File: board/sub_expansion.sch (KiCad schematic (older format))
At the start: 0 parts

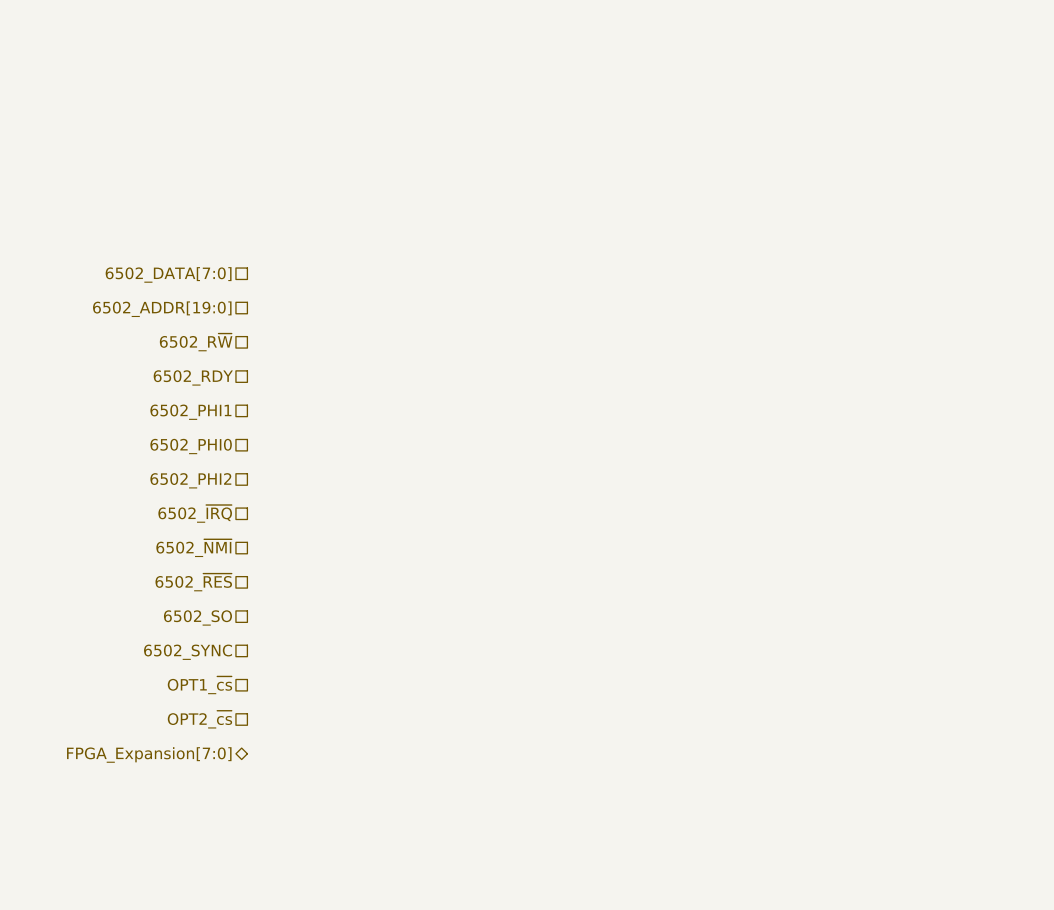
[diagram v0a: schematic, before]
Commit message: Level converters complete, display almost done
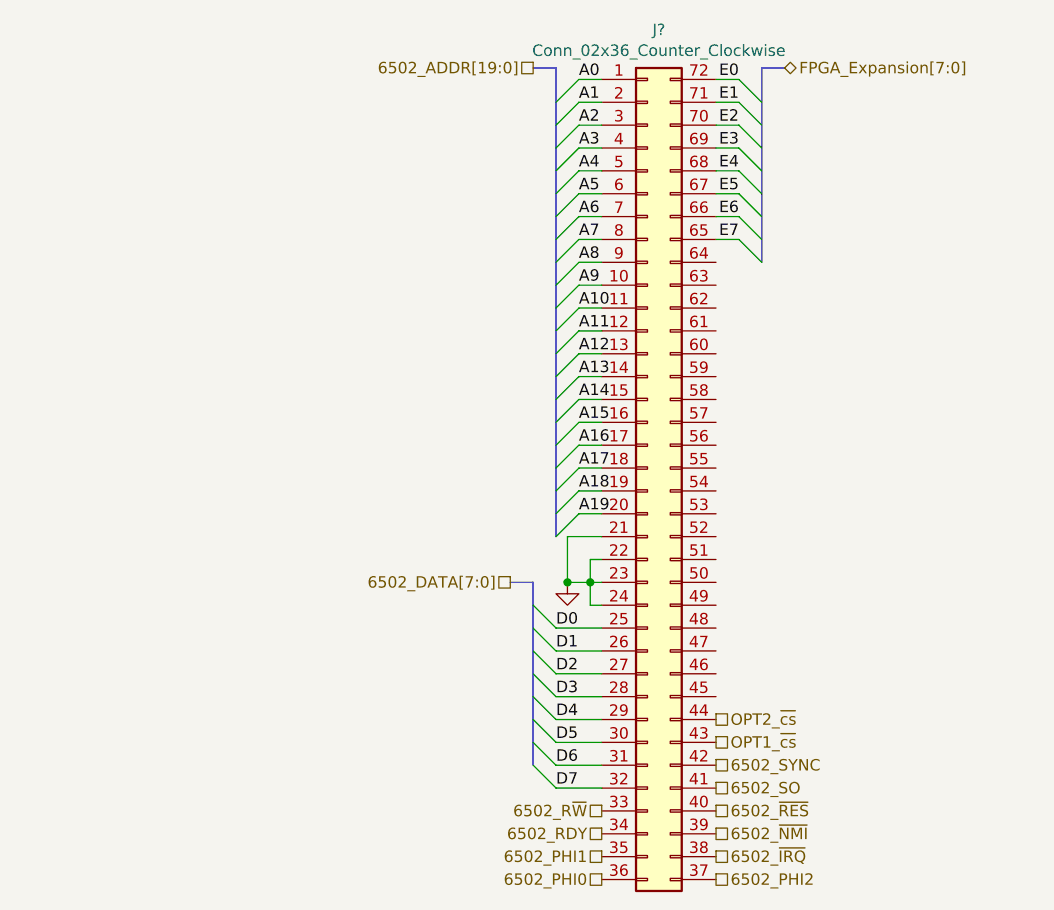
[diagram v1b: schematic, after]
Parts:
- added J?: Conn_02x36_Counter_Clockwise, symbol Connector_Generic:Conn_02x36_Counter_Clockwise
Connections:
- net 6502_PHI0: now also J?.36 (Pin_36)
- net 6502_PHI1: now also J?.35 (Pin_35)
- net 6502_PHI2: now also J?.37 (Pin_37)
- net 6502_RDY: now also J?.34 (Pin_34)
- net 6502_R~W: now also J?.33 (Pin_33)
- net 6502_SO: now also J?.41 (Pin_41)
- net 6502_SYNC: now also J?.42 (Pin_42)
- net 6502_~IRQ: now also J?.38 (Pin_38)
- net 6502_~NMI: now also J?.39 (Pin_39)
- net 6502_~RES: now also J?.40 (Pin_40)
- net OPT1_~cs: now also J?.43 (Pin_43)
- net OPT2_~cs: now also J?.44 (Pin_44)
- new net A0: J?.1 (Pin_1)
- new net A1: J?.2 (Pin_2)
- new net A10: J?.11 (Pin_11)
- new net A11: J?.12 (Pin_12)
- new net A12: J?.13 (Pin_13)
- new net A13: J?.14 (Pin_14)
- new net A14: J?.15 (Pin_15)
- new net A15: J?.16 (Pin_16)
- new net A16: J?.17 (Pin_17)
- new net A17: J?.18 (Pin_18)
- new net A18: J?.19 (Pin_19)
- new net A19: J?.20 (Pin_20)
- new net A2: J?.3 (Pin_3)
- new net A3: J?.4 (Pin_4)
- new net A4: J?.5 (Pin_5)
- new net A5: J?.6 (Pin_6)
- new net A6: J?.7 (Pin_7)
- new net A7: J?.8 (Pin_8)
- new net A8: J?.9 (Pin_9)
- new net A9: J?.10 (Pin_10)
- new net D0: J?.25 (Pin_25)
- new net D1: J?.26 (Pin_26)
- new net D2: J?.27 (Pin_27)
- new net D3: J?.28 (Pin_28)
- new net D4: J?.29 (Pin_29)
- new net D5: J?.30 (Pin_30)
- new net D6: J?.31 (Pin_31)
- new net D7: J?.32 (Pin_32)
- new net E0: J?.72 (Pin_72)
- new net E1: J?.71 (Pin_71)
- new net E2: J?.70 (Pin_70)
- new net E3: J?.69 (Pin_69)
- new net E4: J?.68 (Pin_68)
- new net E5: J?.67 (Pin_67)
- new net E6: J?.66 (Pin_66)
- new net E7: J?.65 (Pin_65)
- new net GND: J?.21 (Pin_21), J?.22 (Pin_22), J?.23 (Pin_23), J?.24 (Pin_24)

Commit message: More Schematic progress
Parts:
- gave numbers to parts that had none: 1
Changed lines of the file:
@@
 $Descr A4 11693 8268
 encoding utf-8
-Sheet 11 15
+Sheet 10 14
 Title ""
 Date ""
@@
 FPGA_Expansion[7:0]
 $Comp
-L Connector_Generic:Conn_02x36_Counter_Clockwise J?
+L Connector_Generic:Conn_02x36_Counter_Clockwise J1001
 U 1 1 5AB66C6D
 P 5950 4400
-F 0 "J?" H 6000 6317 50  0000 C CNN
+F 0 "J1001" H 6000 6317 50  0000 C CNN
 F 1 "Conn_02x36_Counter_Clockwise" H 6000 6226 50  0000 C CNN
 F 2 "" H 5950 4400 50  0001 C CNN
@@
 	5350 4900 5450 4900
 $Comp
-L power:GND #PWR?
+L power:GND #PWR01001
 U 1 1 5AB6DD73
 P 5600 4900
-F 0 "#PWR?" H 5600 4650 50  0001 C CNN
+F 0 "#PWR01001" H 5600 4650 50  0001 C CNN
 F 1 "GND" H 5500 5000 50  0001 C CNN
 F 2 "" H 5600 4900 50  0001 C CNN
@@
 	6450 2650 6550 2650
 Wire Bus Line
+	6450 2650 6450 3500
+Wire Bus Line
 	5450 4900 5450 5700
 Wire Bus Line
-	6450 2650 6450 3500
-Wire Bus Line
 	5550 2650 5550 4700

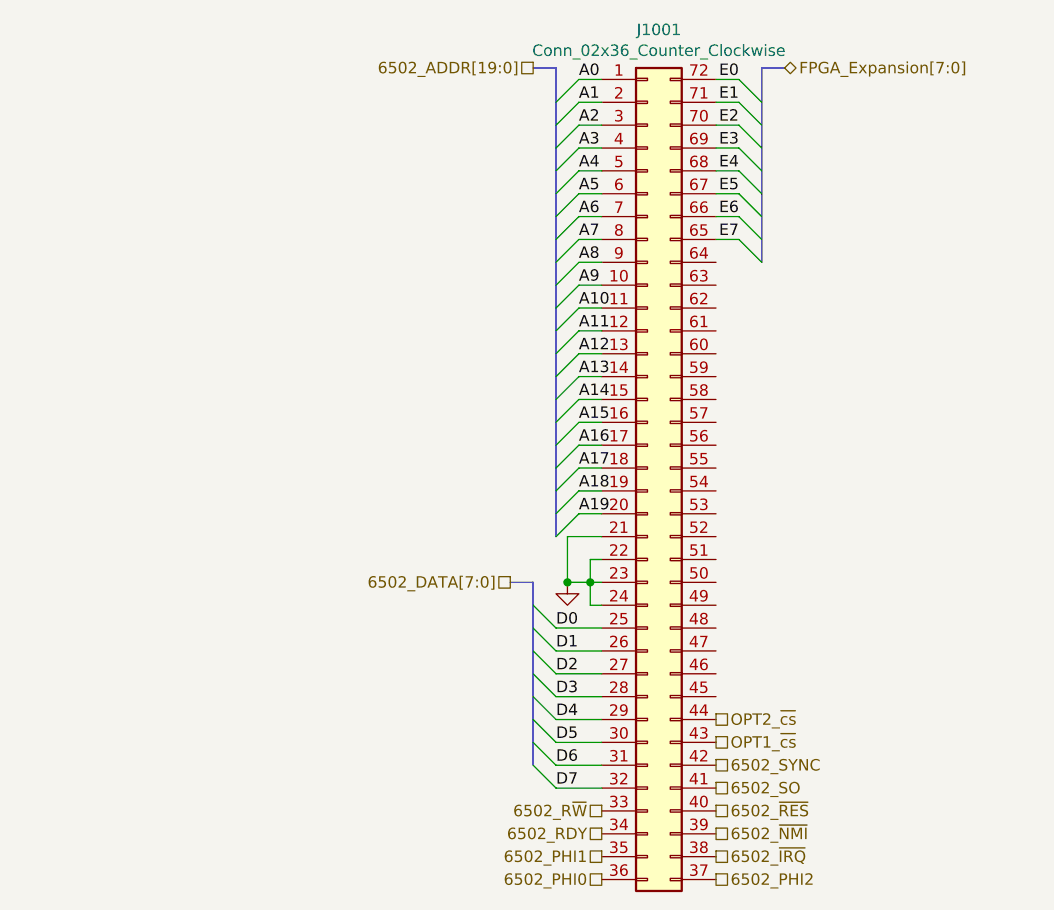
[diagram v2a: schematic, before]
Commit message: Bus signal connectivity rebuilt
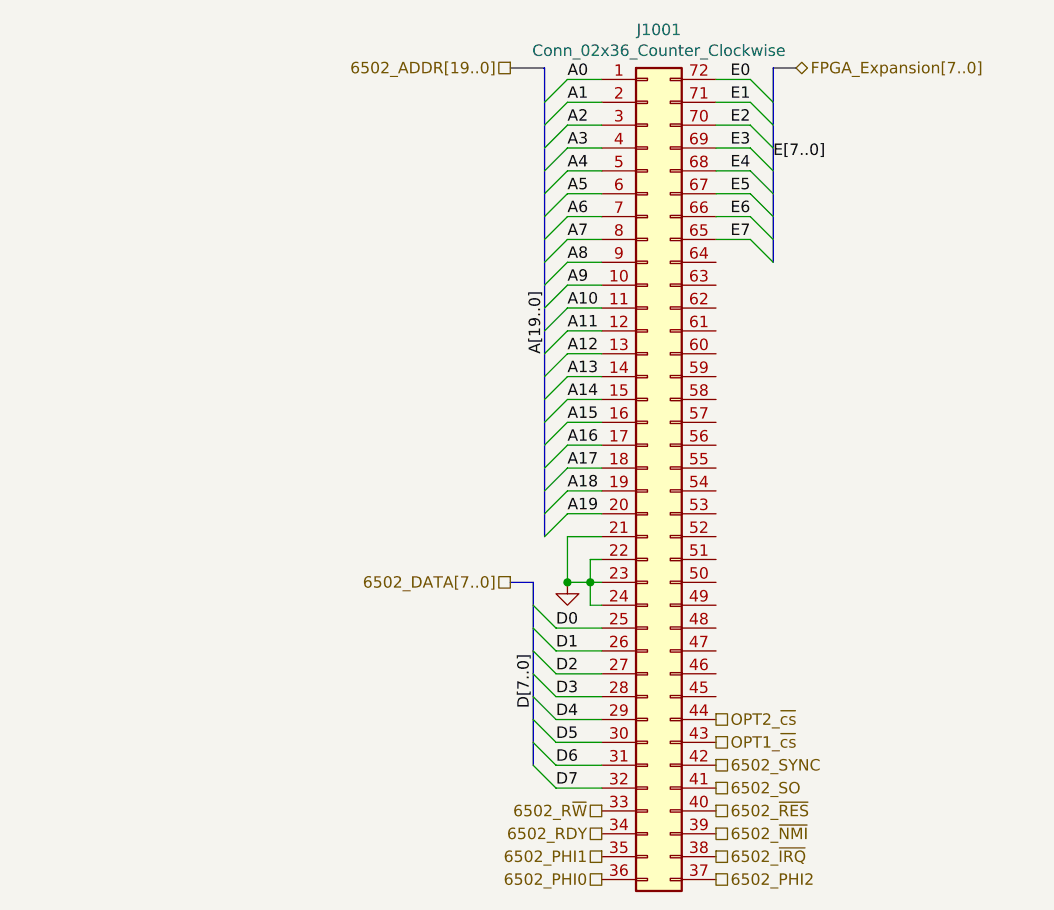
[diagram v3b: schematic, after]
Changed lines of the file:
@@
 $EndDescr
 Text HLabel 5350 4900 0    50   UnSpc ~ 0
-6502_DATA[7:0]
-Text HLabel 5450 2650 0    50   UnSpc ~ 0
-6502_ADDR[19:0]
+6502_DATA[7..0]
+Text HLabel 5350 2650 0    50   UnSpc ~ 0
+6502_ADDR[19..0]
 Text HLabel 5750 5900 0    50   UnSpc ~ 0
 6502_R~W
@@
 Text HLabel 6250 5700 2    50   UnSpc ~ 0
 6502_SYNC
-Text HLabel 6550 2650 2    50   BiDi ~ 0
-FPGA_Expansion[7:0]
+Text HLabel 6600 2650 2    50   BiDi ~ 0
+FPGA_Expansion[7..0]
 $Comp
 L Connector_Generic:Conn_02x36_Counter_Clockwise J1001
@@
 	5550 5800 5450 5700
 Entry Wire Line
-	5650 3900 5550 4000
-Entry Wire Line
-	5650 4000 5550 4100
-Entry Wire Line
-	5650 4100 5550 4200
-Entry Wire Line
-	5550 3900 5650 3800
-Entry Wire Line
-	5550 3800 5650 3700
-Entry Wire Line
-	5550 3700 5650 3600
-Entry Wire Line
-	5550 3600 5650 3500
-Entry Wire Line
-	5550 3300 5650 3200
-Entry Wire Line
-	5550 3200 5650 3100
-Entry Wire Line
-	5550 3100 5650 3000
-Entry Wire Line
-	5550 3000 5650 2900
-Entry Wire Line
-	5550 2900 5650 2800
-Entry Wire Line
-	5550 2800 5650 2700
-Entry Wire Line
-	5550 3400 5650 3300
-Entry Wire Line
-	5550 3500 5650 3400
-Text Label 5650 3900 0    50   ~ 0
+	5600 3900 5500 4000
+Entry Wire Line
+	5600 4000 5500 4100
+Entry Wire Line
+	5600 4100 5500 4200
+Entry Wire Line
+	5500 3900 5600 3800
+Entry Wire Line
+	5500 3800 5600 3700
+Entry Wire Line
+	5500 3700 5600 3600
+Entry Wire Line
+	5500 3600 5600 3500
+Entry Wire Line
+	5500 3300 5600 3200
+Entry Wire Line
+	5500 3200 5600 3100
+Entry Wire Line
+	5500 3100 5600 3000
+Entry Wire Line
+	5500 3000 5600 2900
+Entry Wire Line
+	5500 2900 5600 2800
+Entry Wire Line
+	5500 2800 5600 2700
+Entry Wire Line
+	5500 3400 5600 3300
+Entry Wire Line
+	5500 3500 5600 3400
+Text Label 5600 3900 0    50   ~ 0
 A12
-Text Label 5650 4000 0    50   ~ 0
+Text Label 5600 4000 0    50   ~ 0
 A13
-Text Label 5650 4100 0    50   ~ 0
+Text Label 5600 4100 0    50   ~ 0
 A14
-Text Label 5650 4200 0    50   ~ 0
+Text Label 5600 4200 0    50   ~ 0
 A15
-Text Label 5650 2700 0    50   ~ 0
+Text Label 5600 2700 0    50   ~ 0
 A0
-Text Label 5650 2800 0    50   ~ 0
+Text Label 5600 2800 0    50   ~ 0
 A1
-Text Label 5650 2900 0    50   ~ 0
+Text Label 5600 2900 0    50   ~ 0
 A2
-Text Label 5650 3000 0    50   ~ 0
+Text Label 5600 3000 0    50   ~ 0
 A3
-Text Label 5650 3100 0    50   ~ 0
+Text Label 5600 3100 0    50   ~ 0
 A4
-Text Label 5650 3200 0    50   ~ 0
+Text Label 5600 3200 0    50   ~ 0
 A5
-Text Label 5650 3300 0    50   ~ 0
+Text Label 5600 3300 0    50   ~ 0
 A6
-Text Label 5650 3500 0    50   ~ 0
+Text Label 5600 3500 0    50   ~ 0
 A8
-Text Label 5650 3400 0    50   ~ 0
+Text Label 5600 3400 0    50   ~ 0
 A7
-Text Label 5650 3600 0    50   ~ 0
+Text Label 5600 3600 0    50   ~ 0
 A9
-Text Label 5650 3700 0    50   ~ 0
+Text Label 5600 3700 0    50   ~ 0
 A10
-Text Label 5650 3800 0    50   ~ 0
+Text Label 5600 3800 0    50   ~ 0
 A11
 Wire Wire Line
-	5650 3900 5750 3900
-Wire Wire Line
-	5750 4000 5650 4000
-Wire Wire Line
-	5650 4100 5750 4100
-Wire Wire Line
-	5750 4200 5650 4200
-Wire Wire Line
-	5750 3800 5650 3800
-Wire Wire Line
-	5650 3700 5750 3700
-Wire Wire Line
-	5750 3600 5650 3600
-Wire Wire Line
-	5650 3500 5750 3500
-Wire Wire Line
-	5750 3400 5650 3400
-Wire Wire Line
-	5650 3300 5750 3300
-Wire Wire Line
-	5750 3200 5650 3200
-Wire Wire Line
-	5650 3100 5750 3100
-Wire Wire Line
-	5750 3000 5650 3000
-Wire Wire Line
-	5650 2900 5750 2900
-Wire Wire Line
-	5750 2800 5650 2800
-Wire Wire Line
-	5650 2700 5750 2700
+	5600 3900 5750 3900
+Wire Wire Line
+	5750 4000 5600 4000
+Wire Wire Line
+	5600 4100 5750 4100
+Wire Wire Line
+	5750 4200 5600 4200
+Wire Wire Line
+	5750 3800 5600 3800
+Wire Wire Line
+	5600 3700 5750 3700
+Wire Wire Line
+	5750 3600 5600 3600
+Wire Wire Line
+	5600 3500 5750 3500
+Wire Wire Line
+	5750 3400 5600 3400
+Wire Wire Line
+	5600 3300 5750 3300
+Wire Wire Line
+	5750 3200 5600 3200
+Wire Wire Line
+	5600 3100 5750 3100
+Wire Wire Line
+	5750 3000 5600 3000
+Wire Wire Line
+	5600 2900 5750 2900
+Wire Wire Line
+	5750 2800 5600 2800
+Wire Wire Line
+	5600 2700 5750 2700
 Wire Wire Line
 	5550 5800 5750 5800
@@
 D7
 Entry Wire Line
-	5650 4300 5550 4400
-Entry Wire Line
-	5650 4400 5550 4500
-Entry Wire Line
-	5650 4500 5550 4600
-Entry Wire Line
-	5650 4600 5550 4700
-Entry Wire Line
-	5550 4300 5650 4200
-Text Label 5650 4300 0    50   ~ 0
+	5600 4300 5500 4400
+Entry Wire Line
+	5600 4400 5500 4500
+Entry Wire Line
+	5600 4500 5500 4600
+Entry Wire Line
+	5600 4600 5500 4700
+Entry Wire Line
+	5500 4300 5600 4200
+Text Label 5600 4300 0    50   ~ 0
 A16
-Text Label 5650 4400 0    50   ~ 0
+Text Label 5600 4400 0    50   ~ 0
 A17
-Text Label 5650 4500 0    50   ~ 0
+Text Label 5600 4500 0    50   ~ 0
 A18
-Text Label 5650 4600 0    50   ~ 0
+Text Label 5600 4600 0    50   ~ 0
 A19
 Wire Wire Line
-	5650 4300 5750 4300
-Wire Wire Line
-	5750 4400 5650 4400
-Wire Wire Line
-	5650 4500 5750 4500
-Wire Wire Line
-	5750 4600 5650 4600
-Wire Bus Line
-	5450 2650 5550 2650
+	5600 4300 5750 4300
+Wire Wire Line
+	5750 4400 5600 4400
+Wire Wire Line
+	5600 4500 5750 4500
+Wire Wire Line
+	5750 4600 5600 4600
 Wire Bus Line
 	5350 4900 5450 4900
@@
 Connection ~ 5600 4900
 Entry Wire Line
-	6450 3300 6350 3200
-Entry Wire Line
-	6450 3200 6350 3100
-Entry Wire Line
-	6450 3100 6350 3000
-Entry Wire Line
-	6450 3000 6350 2900
-Entry Wire Line
-	6450 2900 6350 2800
-Entry Wire Line
-	6450 2800 6350 2700
-Entry Wire Line
-	6450 3400 6350 3300
-Entry Wire Line
-	6450 3500 6350 3400
-Text Label 6350 2700 2    50   ~ 0
+	6500 3300 6400 3200
+Entry Wire Line
+	6500 3200 6400 3100
+Entry Wire Line
+	6500 3100 6400 3000
+Entry Wire Line
+	6500 3000 6400 2900
+Entry Wire Line
+	6500 2900 6400 2800
+Entry Wire Line
+	6500 2800 6400 2700
+Entry Wire Line
+	6500 3400 6400 3300
+Entry Wire Line
+	6500 3500 6400 3400
+Text Label 6400 2700 2    50   ~ 0
 E0
-Text Label 6350 2800 2    50   ~ 0
+Text Label 6400 2800 2    50   ~ 0
 E1
-Text Label 6350 2900 2    50   ~ 0
+Text Label 6400 2900 2    50   ~ 0
 E2
-Text Label 6350 3000 2    50   ~ 0
+Text Label 6400 3000 2    50   ~ 0
 E3
-Text Label 6350 3100 2    50   ~ 0
+Text Label 6400 3100 2    50   ~ 0
 E4
-Text Label 6350 3200 2    50   ~ 0
+Text Label 6400 3200 2    50   ~ 0
 E5
-Text Label 6350 3300 2    50   ~ 0
+Text Label 6400 3300 2    50   ~ 0
 E6
-Text Label 6350 3400 2    50   ~ 0
+Text Label 6400 3400 2    50   ~ 0
 E7
 Wire Wire Line
-	6250 3400 6350 3400
-Wire Wire Line
-	6350 3300 6250 3300
-Wire Wire Line
-	6250 3200 6350 3200
-Wire Wire Line
-	6350 3100 6250 3100
-Wire Wire Line
-	6250 3000 6350 3000
-Wire Wire Line
-	6350 2900 6250 2900
-Wire Wire Line
-	6250 2800 6350 2800
-Wire Wire Line
-	6350 2700 6250 2700
-Wire Bus Line
-	6450 2650 6550 2650
-Wire Bus Line
-	6450 2650 6450 3500
+	6250 3400 6400 3400
+Wire Wire Line
+	6400 3300 6250 3300
+Wire Wire Line
+	6250 3200 6400 3200
+Wire Wire Line
+	6400 3100 6250 3100
+Wire Wire Line
+	6250 3000 6400 3000
+Wire Wire Line
+	6400 2900 6250 2900
+Wire Wire Line
+	6250 2800 6400 2800
+Wire Wire Line
+	6400 2700 6250 2700
+Wire Bus Line
+	6500 2650 6600 2650
+Wire Bus Line
+	5500 2650 5350 2650
+Text Label 5500 3900 1    50   ~ 0
+A[19..0]
+Wire Bus Line
+	6500 2650 6500 3500
 Wire Bus Line
 	5450 4900 5450 5700
 Wire Bus Line
-	5550 2650 5550 4700
+	5500 2650 5500 4700
+Text Label 6500 3050 0    50   ~ 0
+E[7..0]
+Text Label 5450 5450 1    50   ~ 0
+D[7..0]
 $EndSCHEMATC

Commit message: Schematics mostly complete
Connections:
- no-connect marks 0 -> 20
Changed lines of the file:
@@
 Text Label 5450 5450 1    50   ~ 0
 D[7..0]
+NoConn ~ 6250 3500
+NoConn ~ 6250 3600
+NoConn ~ 6250 3700
+NoConn ~ 6250 3800
+NoConn ~ 6250 3900
+NoConn ~ 6250 4000
+NoConn ~ 6250 4100
+NoConn ~ 6250 4200
+NoConn ~ 6250 4300
+NoConn ~ 6250 4400
+NoConn ~ 6250 4500
+NoConn ~ 6250 4600
+NoConn ~ 6250 4700
+NoConn ~ 6250 4800
+NoConn ~ 6250 4900
+NoConn ~ 6250 5000
+NoConn ~ 6250 5100
+NoConn ~ 6250 5200
+NoConn ~ 6250 5300
+NoConn ~ 6250 5400
 Wire Bus Line
 	6500 2650 6500 3500

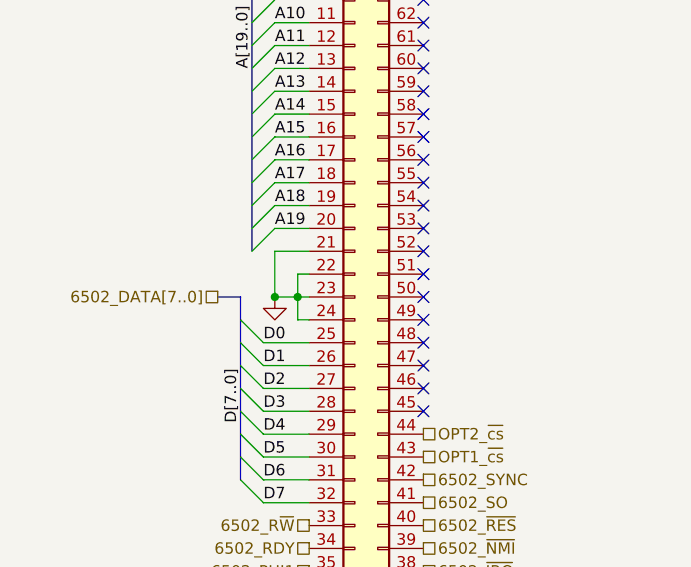
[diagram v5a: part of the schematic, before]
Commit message: Started picking footprints. Merged many components.
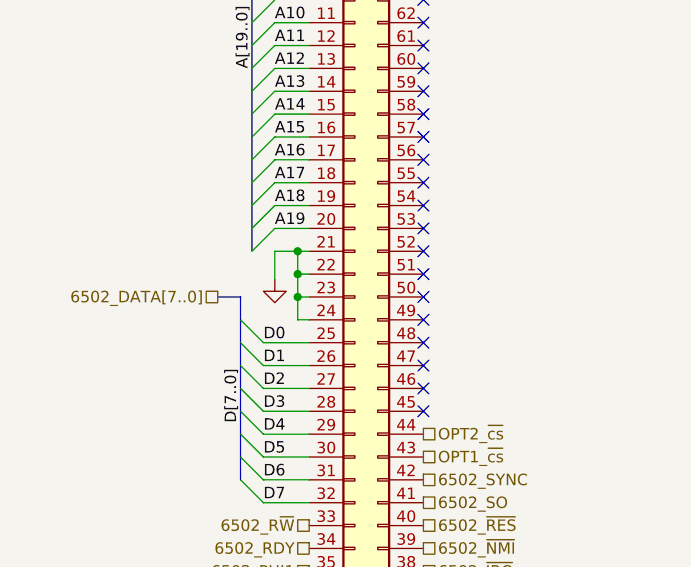
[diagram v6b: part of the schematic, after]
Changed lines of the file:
@@
 $Descr A4 11693 8268
 encoding utf-8
-Sheet 10 14
+Sheet 10 15
 Title ""
 Date ""
@@
 L power:GND #PWR01001
 U 1 1 5AB6DD73
-P 5600 4900
-F 0 "#PWR01001" H 5600 4650 50  0001 C CNN
-F 1 "GND" H 5500 5000 50  0001 C CNN
-F 2 "" H 5600 4900 50  0001 C CNN
-F 3 "" H 5600 4900 50  0001 C CNN
-	1    5600 4900
+P 5600 4825
+F 0 "#PWR01001" H 5600 4575 50  0001 C CNN
+F 1 "GND" H 5500 4925 50  0001 C CNN
+F 2 "" H 5600 4825 50  0001 C CNN
+F 3 "" H 5600 4825 50  0001 C CNN
+	1    5600 4825
 	1    0    0    -1
 $EndComp
 Wire Wire Line
-	5750 4700 5600 4700
+	5750 4700 5700 4700
 Wire Wire Line
 	5750 5000 5700 5000
@@
 	5700 4800 5700 4900
 Wire Wire Line
-	5600 4700 5600 4900
-Wire Wire Line
-	5600 4900 5700 4900
-Connection ~ 5600 4900
+	5600 4700 5600 4825
 Entry Wire Line
 	6500 3300 6400 3200
@@
 NoConn ~ 6250 5300
 NoConn ~ 6250 5400
+Wire Wire Line
+	5700 4800 5700 4700
+Connection ~ 5700 4800
+Connection ~ 5700 4700
+Wire Wire Line
+	5700 4700 5600 4700
 Wire Bus Line
 	6500 2650 6500 3500
